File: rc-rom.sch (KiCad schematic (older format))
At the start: 20 parts, among them J1 RC2014, J2 RC2014_Enh, U1 27C512, U2 74HCT138, U3 74HCT74, U4 74HCT4075

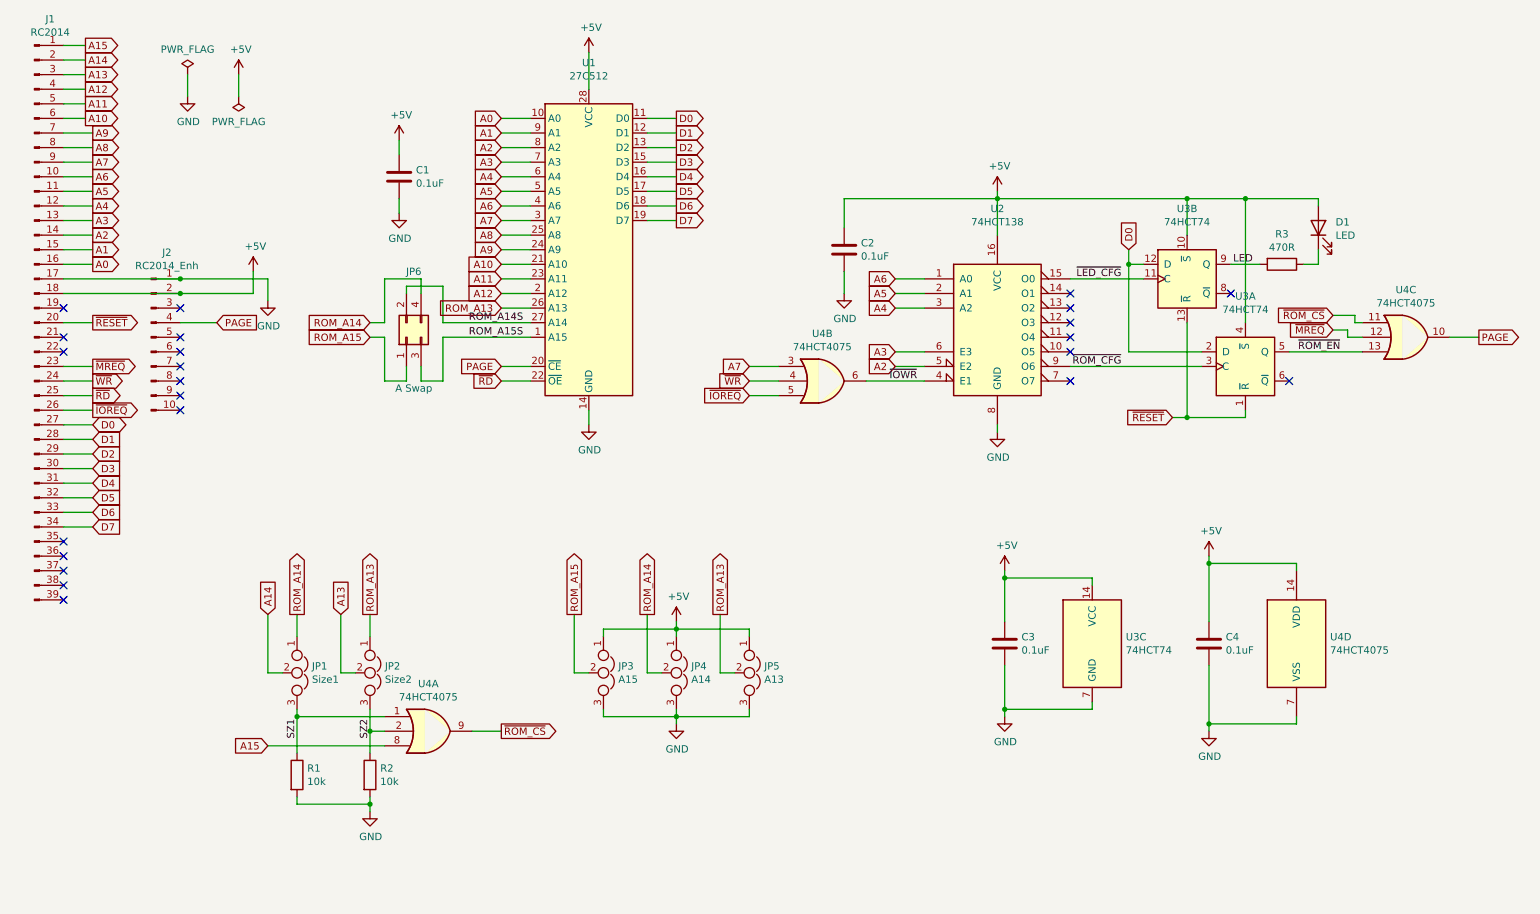
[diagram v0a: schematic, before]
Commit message: Added silkscreen jumper diagrams, tweaked net labels
Added reference diagrams for jumpers on the silkscreen, tweaked net labels
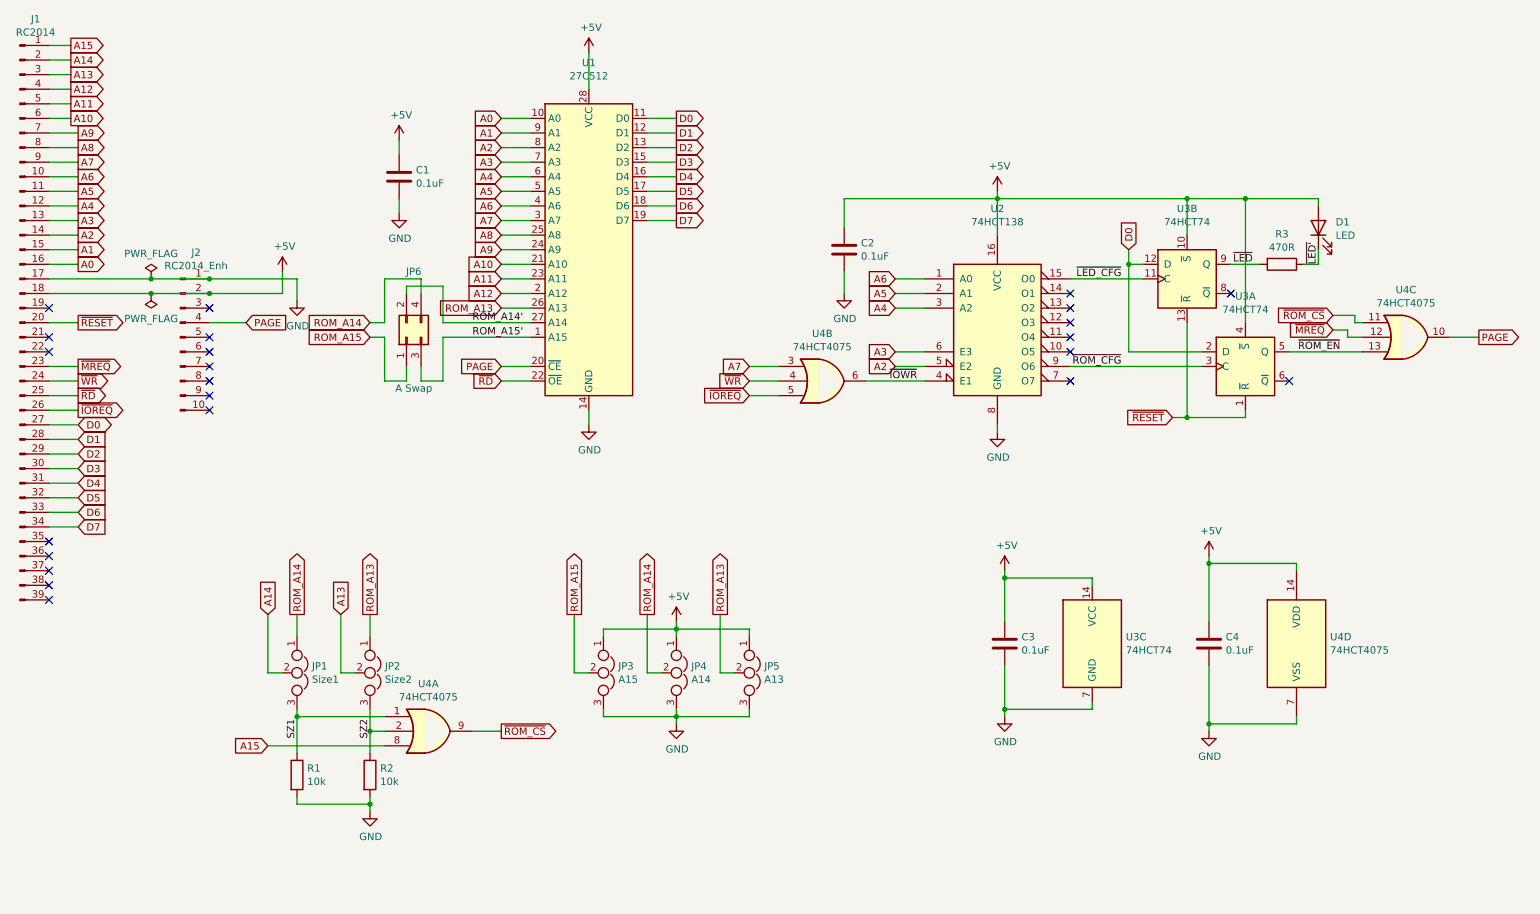
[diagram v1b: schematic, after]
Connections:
- net ~LED': now reaches D1.1 (K), R3.1
- net LED renamed ~LED
- net ROM_A14S renamed ROM_A14'
- net ROM_A15S renamed ROM_A15'
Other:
- moved on the sheet: J1, J2

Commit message: Added README, tidied up schematic and board
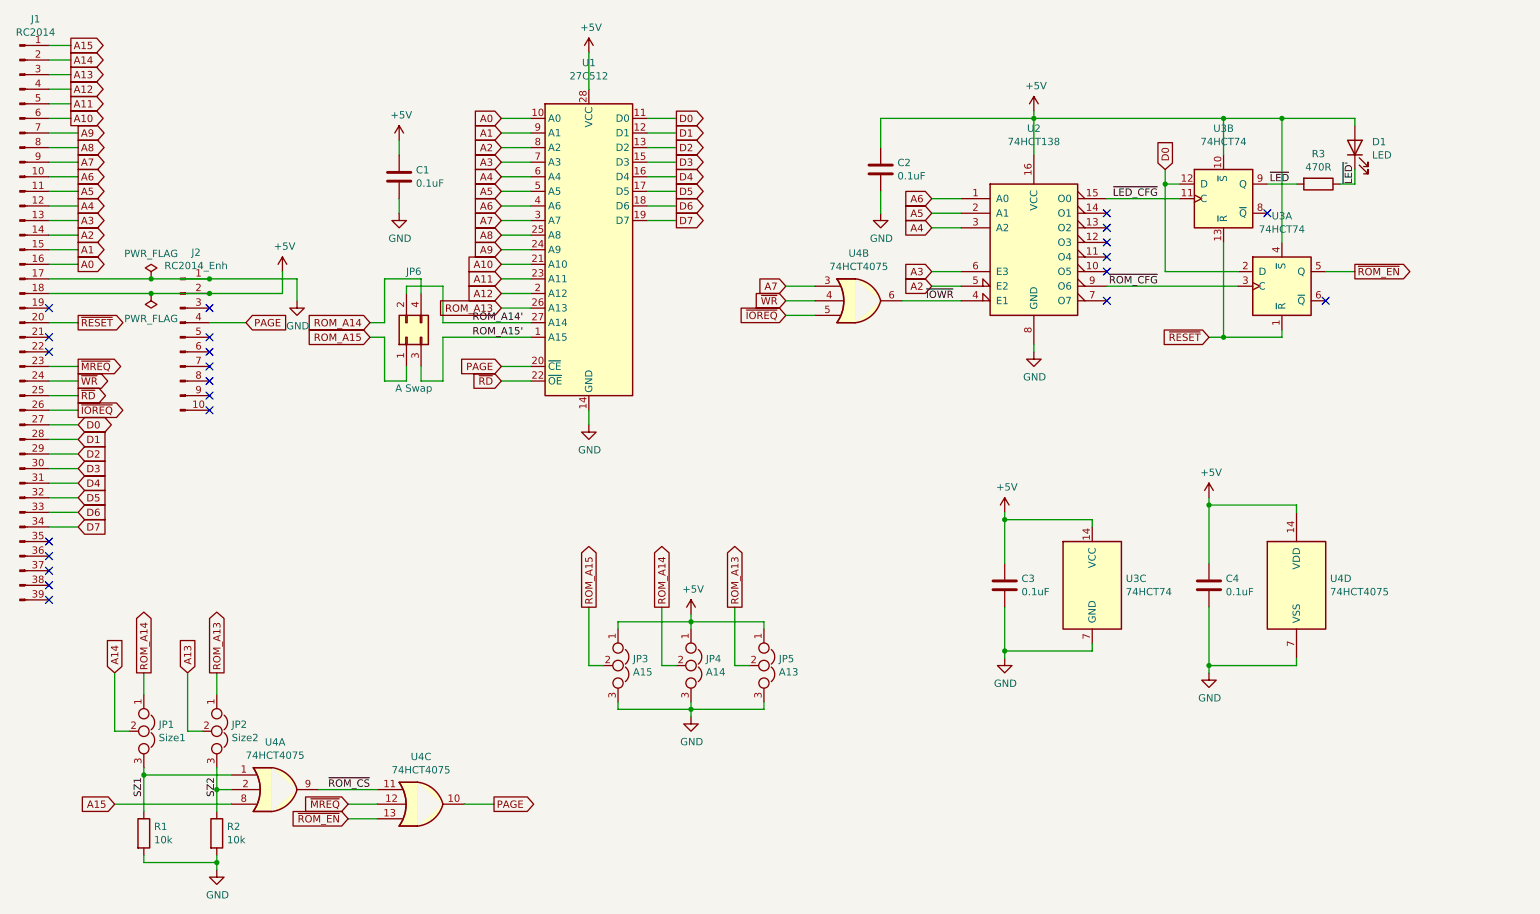
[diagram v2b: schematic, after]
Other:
- moved on the sheet: C2, C3, C4, D1, JP1, JP2, JP3, JP4, JP5, R1, R2, R3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

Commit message: Moved to version 1.1, added LED for paging status
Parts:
- added D2: Green, LED_THT:LED_D3.0mm, symbol Device:LED
- added R4: 470R, Resistor_THT:R_Axial_DIN0207_L6.3mm_D2.5mm_P7.62mm_Horizontal, symbol Device:R
- D1: value LED -> Yellow
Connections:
- net +5V: now also D2.2 (A)
- net ~Paged: now reaches U3.6 (~Q)
- net ~Paged: now also R4.1
- new net ~Paged': D2.1 (K), R4.2
- no-connect marks 23 -> 22
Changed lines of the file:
@@
 Wire Wire Line
 	9400 3250 9400 3200
-NoConn ~ 9700 3000
 $Comp
 L power:GND #PWR0104
@@
 P 9900 1950
 F 0 "D1" V 9939 1832 50  0000 R CNN
-F 1 "LED" V 9848 1832 50  0000 R CNN
+F 1 "Yellow" V 9848 1832 50  0000 R CNN
 F 2 "LED_THT:LED_D3.0mm" H 9900 1950 50  0001 C CNN
 F 3 "~" H 9900 1950 50  0001 C CNN
@@
 Text Label 3150 6350 2    50   ~ 0
 ~ROM_CS
+$Comp
+L Device:R R4
+U 1 1 5FE8CC92
+P 10300 2550
+F 0 "R4" V 10093 2550 50  0000 C CNN
+F 1 "470R" V 10184 2550 50  0000 C CNN
+F 2 "Resistor_THT:R_Axial_DIN0207_L6.3mm_D2.5mm_P7.62mm_Horizontal" V 10230 2550 50  0001 C CNN
+F 3 "~" H 10300 2550 50  0001 C CNN
+	1    10300 2550
+	-1   0    0    1
+$EndComp
+$Comp
+L Device:LED D2
+U 1 1 5FE8D4DA
+P 10300 1950
+F 0 "D2" V 10339 1832 50  0000 R CNN
+F 1 "Green" V 10248 1832 50  0000 R CNN
+F 2 "LED_THT:LED_D3.0mm" H 10300 1950 50  0001 C CNN
+F 3 "~" H 10300 1950 50  0001 C CNN
+	1    10300 1950
+	0    -1   -1   0
+$EndComp
+Wire Wire Line
+	9900 1750 10300 1750
+Wire Wire Line
+	10300 1750 10300 1800
+Connection ~ 9900 1750
+Wire Wire Line
+	10300 2100 10300 2400
+Wire Wire Line
+	10300 2700 10300 3000
+Wire Wire Line
+	10300 3000 9700 3000
+Text Label 10200 3000 2    50   ~ 0
+~Paged
+Text Label 10300 2350 1    50   ~ 0
+~Paged'
 $EndSCHEMATC
